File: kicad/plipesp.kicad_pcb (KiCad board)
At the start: 2 copper layers, 38 x 35.5 mm, 37 parts, among them CON1 IEEEE-1284A, J1 USB_B_Micro, J2 Conn_01x04_Male, J3 Conn_01x06_Male, J4 Micro_SD_Card_Det, U1 AMS1117-3.3, U2 CBTD3384, U3 CBTD3384, U4 ESP32-WROOM-32D

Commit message: board rev2
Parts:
- added REF4: mounting_hole, plipesp:mounting_hole, F.Cu at (123.0, 127.3)
- C3, C4: footprint Capacitor_SMD:C_0805_2012Metric -> Capacitor_SMD:C_1206_3216Metric
- J1: footprint Connector_USB:USB_Micro-B_Amphenol_10103594-0001LF_Horizontal -> plipesp:USB_Micro-B_Amphenol_10103594-0001LF_Horizontal
- U2, U3: footprint Package_SO:TSSOP-24_4.4x7.8mm_P0.65mm -> plipesp:SO-universal-24_P0.65mm
- U4: footprint RF_Module:ESP32-WROOM-32 -> plipesp:ESP32-WROOM-32
- moved R3 19.5 mm to (100.9, 153.0), turned to -90 degrees
- moved C7 19.4 mm to (113.1, 127.0), turned to 90 degrees
- moved R1 19.1 mm to (107.8, 153.0), turned to -90 degrees
- moved R11 18.9 mm to (95.7, 137.1), turned to 0 degrees
- moved R2 18.6 mm to (104.3, 153.0), turned to -90 degrees
- moved R10 15.3 mm to (111.1, 140.4)
- moved D3 14.1 mm to (100.9, 149.2), turned to 90 degrees
- moved D1 13.8 mm to (107.8, 149.2), turned to 90 degrees
- moved R4 13.4 mm to (98.6, 140.4)
- moved D2 13.1 mm to (104.3, 149.2), turned to 90 degrees
- moved REF1 12.2 mm to (84.0, 127.3)
- moved R9 11.1 mm to (108.6, 140.4)
- moved R5 9.48 mm to (101.1, 140.4)
- moved R7 7.87 mm to (106.1, 140.4)
- moved R6 7.14 mm to (103.6, 140.4)
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- renumbered REF** to REF1, REF** to REF2, REF** to REF3
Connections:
- net ~ACK renamed ~{ACK}
- net ~IO_EN renamed ~{IO_EN}
- net ~SD_DETECT1 renamed ~{SD_DETECT1}
- net ~SD_DETECT2 renamed ~{SD_DETECT2}
- net ~STROBE renamed ~{STROBE}
- CON1 pad 15: Net-(CON1-Pad15) -> unconnected-(CON1-Pad15)
- J1 pad 2: Net-(J1-Pad2) -> unconnected-(J1-Pad2)
- J1 pad 3: Net-(J1-Pad3) -> unconnected-(J1-Pad3)
- J1 pad 4: Net-(J1-Pad4) -> unconnected-(J1-Pad4)
- U3 pad 10: Net-(U3-Pad10) -> unconnected-(U3-Pad10)
- U3 pad 11: Net-(U3-Pad11) -> unconnected-(U3-Pad11)
- U3 pad 14: Net-(U3-Pad14) -> unconnected-(U3-Pad14)
- U3 pad 15: Net-(U3-Pad15) -> unconnected-(U3-Pad15)
- U3 pad 16: Net-(U3-Pad16) -> unconnected-(U3-Pad16)
- U3 pad 17: Net-(U3-Pad17) -> unconnected-(U3-Pad17)
- U3 pad 18: Net-(U3-Pad18) -> unconnected-(U3-Pad18)
- U3 pad 19: Net-(U3-Pad19) -> unconnected-(U3-Pad19)
- U3 pad 20: Net-(U3-Pad20) -> unconnected-(U3-Pad20)
- U3 pad 21: Net-(U3-Pad21) -> unconnected-(U3-Pad21)
- U3 pad 22: Net-(U3-Pad22) -> unconnected-(U3-Pad22)
- U3 pad 23: Net-(U3-Pad23) -> unconnected-(U3-Pad23)
- U3 pad 9: ~AMI_RESET -> ~{AMI_RESET}
- U4 pad 11: ~AMI_RESET -> POUT
- U4 pad 32: Net-(U4-Pad32) -> unconnected-(U4-Pad32)
- U4 pad 4: Net-(U4-Pad4) -> unconnected-(U4-Pad4)
- U4 pad 5: Net-(U4-Pad5) -> unconnected-(U4-Pad5)
- U4 pad 9: POUT -> ~{AMI_RESET}
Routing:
- net +5V: track 69.5 -> 123.9 mm, vias 2 -> 0
- net SD_D3: track 10.00 -> 38.9 mm
- net ~{SD_DETECT1}: track 12.4 -> 39.5 mm
- net ~{AMI_RESET}: track 0.00 -> 23.8 mm, vias 0 -> 2
- net SD_D2: track 11.0 -> 32.7 mm
- net +3V3: track 89.9 -> 110.8 mm
- net ~AMI_RESET: track 18.3 -> 0.00 mm, vias 2 -> 0
- net SD_CMD: track 11.0 -> 26.8 mm
- net LED_STATUS2: track 9.38 -> 23.1 mm
- net ~{SD_DETECT2}: track 20.5 -> 8.26 mm
- net GND: track 198.3 -> 186.6 mm, vias 34 -> 22
- net I2C_SDA: track 21.8 -> 33.2 mm
- net SD_D1: track 18.8 -> 27.0 mm, vias 1 -> 2
- net SD_D0: track 13.0 -> 21.1 mm, vias 1 -> 2
- net LED_STATUS: track 14.0 -> 6.45 mm
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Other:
- board size 38 x 35.5 mm -> 44 x 40 mm
- net class Default removed
- net class power removed
- board text added: "3V3"
- board text added: "GND"
- board text added: "JLCJLCJLCJLC"
- board text added: "Rock n Roll doctor Rev. 2"
- board text added: "SCL"
- board text added: "SDA"
- board text removed: "3V"
- board text removed: "CL"
- board text removed: "DA"
- board text removed: "GD"
- board text removed: "Rock n Roll doctor Rev. 1"

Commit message: rev3s - with SD card
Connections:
- U4 pad 11: POUT -> BUSY
- U4 pad 8: BUSY -> ~{AMI_RESET}
- U4 pad 9: ~{AMI_RESET} -> POUT
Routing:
- net ~{AMI_RESET}: track 23.8 -> 30.9 mm
- net BUSY: track 26.1 -> 19.3 mm, vias 0 -> 2
- net POUT: track 20.1 -> 25.5 mm
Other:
- board text added: "Rock n Roll Doctor Rev. 3s"
- board text added: "github.com/AmigaPorts/ImpBox32 The ultimate PLIP by LMC and R3D"
- board text removed: "Rock n Roll doctor Rev. 2"
- board text removed: "github.com/AmigaPorts/ImpBox32 the ultimate PLIP by LMC and R3D"

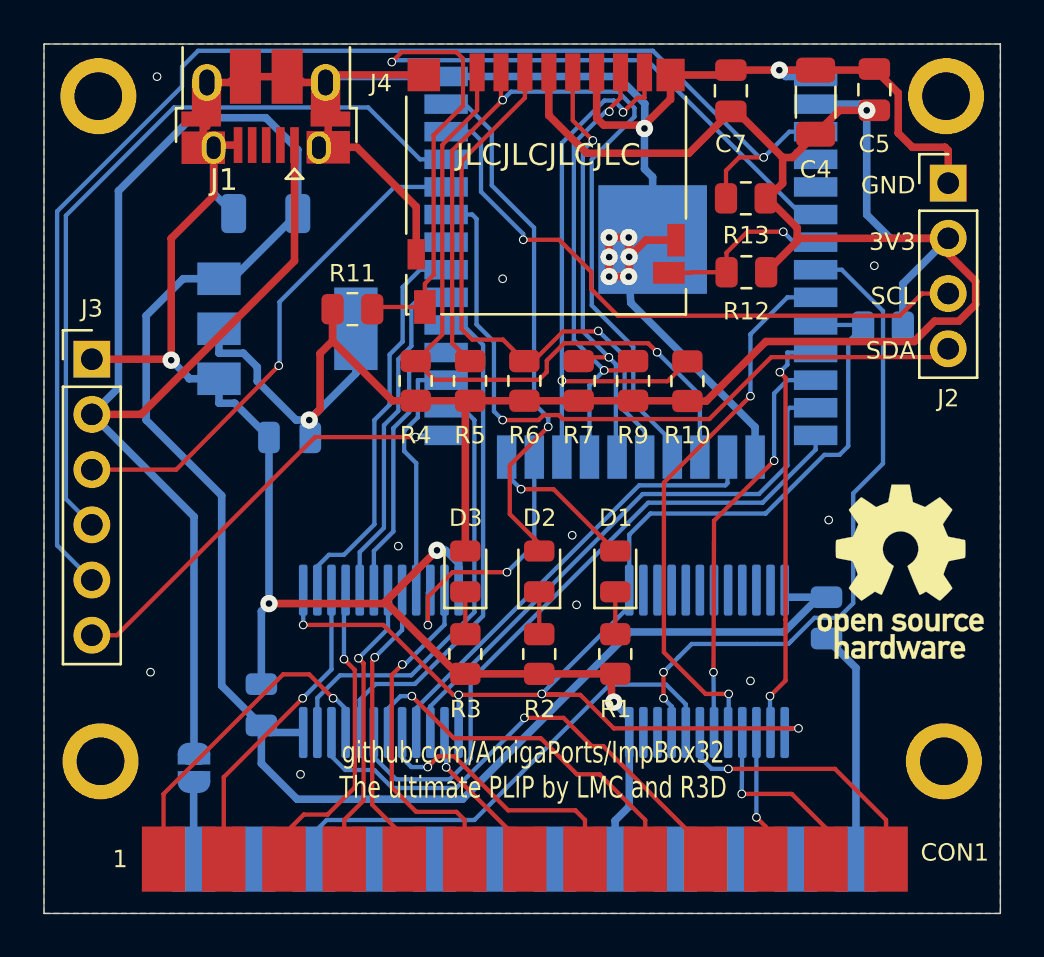
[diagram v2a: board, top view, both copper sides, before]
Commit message: rev3 - without SD card, AMI_RESET optional, extra IO on pins
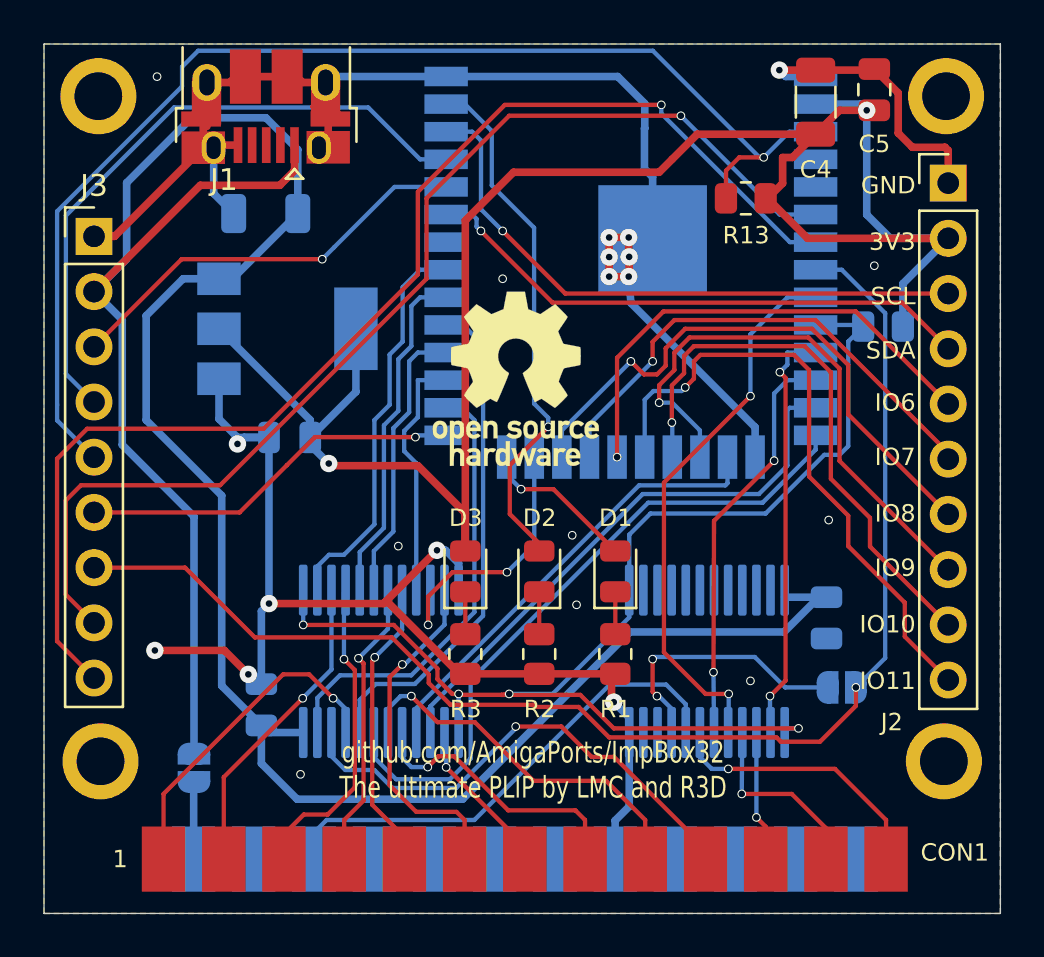
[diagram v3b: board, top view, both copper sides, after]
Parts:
- removed C7: 100nF, Capacitor_SMD:C_0805_2012Metric
- removed J4: Micro_SD_Card_Det, Connector_Card:microSD_HC_Hirose_DM3D-SF
- removed R10, R11, R12, R4, R5, R6, R7, R9: 10k, Resistor_SMD:R_0805_2012Metric
- added JP2: RESET_EN, Jumper:SolderJumper-2_P1.3mm_Open_RoundedPad1.0x1.5mm, B.Cu at (118.2, 154.5)
- J2: footprint Connector_PinHeader_2.54mm:PinHeader_1x04_P2.54mm_Vertical -> Connector_PinHeader_2.54mm:PinHeader_1x10_P2.54mm_Vertical
- J3: footprint Connector_PinHeader_2.54mm:PinHeader_1x06_P2.54mm_Vertical -> Connector_PinHeader_2.54mm:PinHeader_1x09_P2.54mm_Vertical
- moved REF** 19.8 mm to (103.2, 140.3)
- moved J3 5.65 mm to (83.8, 133.8)
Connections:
- U4 pad 17: SD_D2 -> IO9
- U4 pad 18: SD_D3 -> IO10
- U4 pad 19: SD_CMD -> IO11
- U4 pad 20: SD_CLK -> IO6
- U4 pad 21: SD_D0 -> IO7
- U4 pad 22: SD_D1 -> IO8
- U4 pad 6: ~{SD_DETECT1} -> IO34
- U4 pad 7: ~{SD_DETECT2} -> IO35
- U4 pad 8: ~{AMI_RESET} -> IO32
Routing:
- net IO32: track 0.00 -> 61.9 mm, vias 0 -> 1
- net IO35: track 0.00 -> 57.5 mm, vias 0 -> 1
- net IO34: track 0.00 -> 52.1 mm, vias 0 -> 1
- net ~{SD_DETECT1}: track 39.5 -> 0.00 mm, vias 1 -> 0
- net GND: track 186.6 -> 147.2 mm
- net SD_D3: track 38.9 -> 0.00 mm, vias 1 -> 0
- net SD_D2: track 32.7 -> 0.00 mm, vias 1 -> 0
- net IO11: track 0.00 -> 28.7 mm, vias 0 -> 1
- net SD_D1: track 27.0 -> 0.00 mm, vias 2 -> 0
- net SD_CMD: track 26.8 -> 0.00 mm, vias 1 -> 0
- net IO8: track 0.00 -> 26.8 mm, vias 0 -> 1
- net IO10: track 0.00 -> 26.2 mm, vias 0 -> 1
- net IO9: track 0.00 -> 26.0 mm, vias 0 -> 1
- net IO7: track 0.00 -> 23.3 mm, vias 0 -> 1
- net IO6: track 0.00 -> 22.5 mm, vias 0 -> 1
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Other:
- board text added: "IO10"
- board text added: "IO11"
- board text added: "IO32"
- board text added: "IO34"
- board text added: "IO35"
- board text added: "IO6"
- board text added: "IO7"
- board text added: "IO8"
- board text added: "IO9"
- board text added: "Rock n Roll Doctor Rev. 3"
- board text removed: "Rock n Roll Doctor Rev. 3s"
